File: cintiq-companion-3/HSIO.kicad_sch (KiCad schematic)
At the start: 14 parts, among them J3 Bus_M.2_Socket_M, J4 Bus_M.2_Socket_E

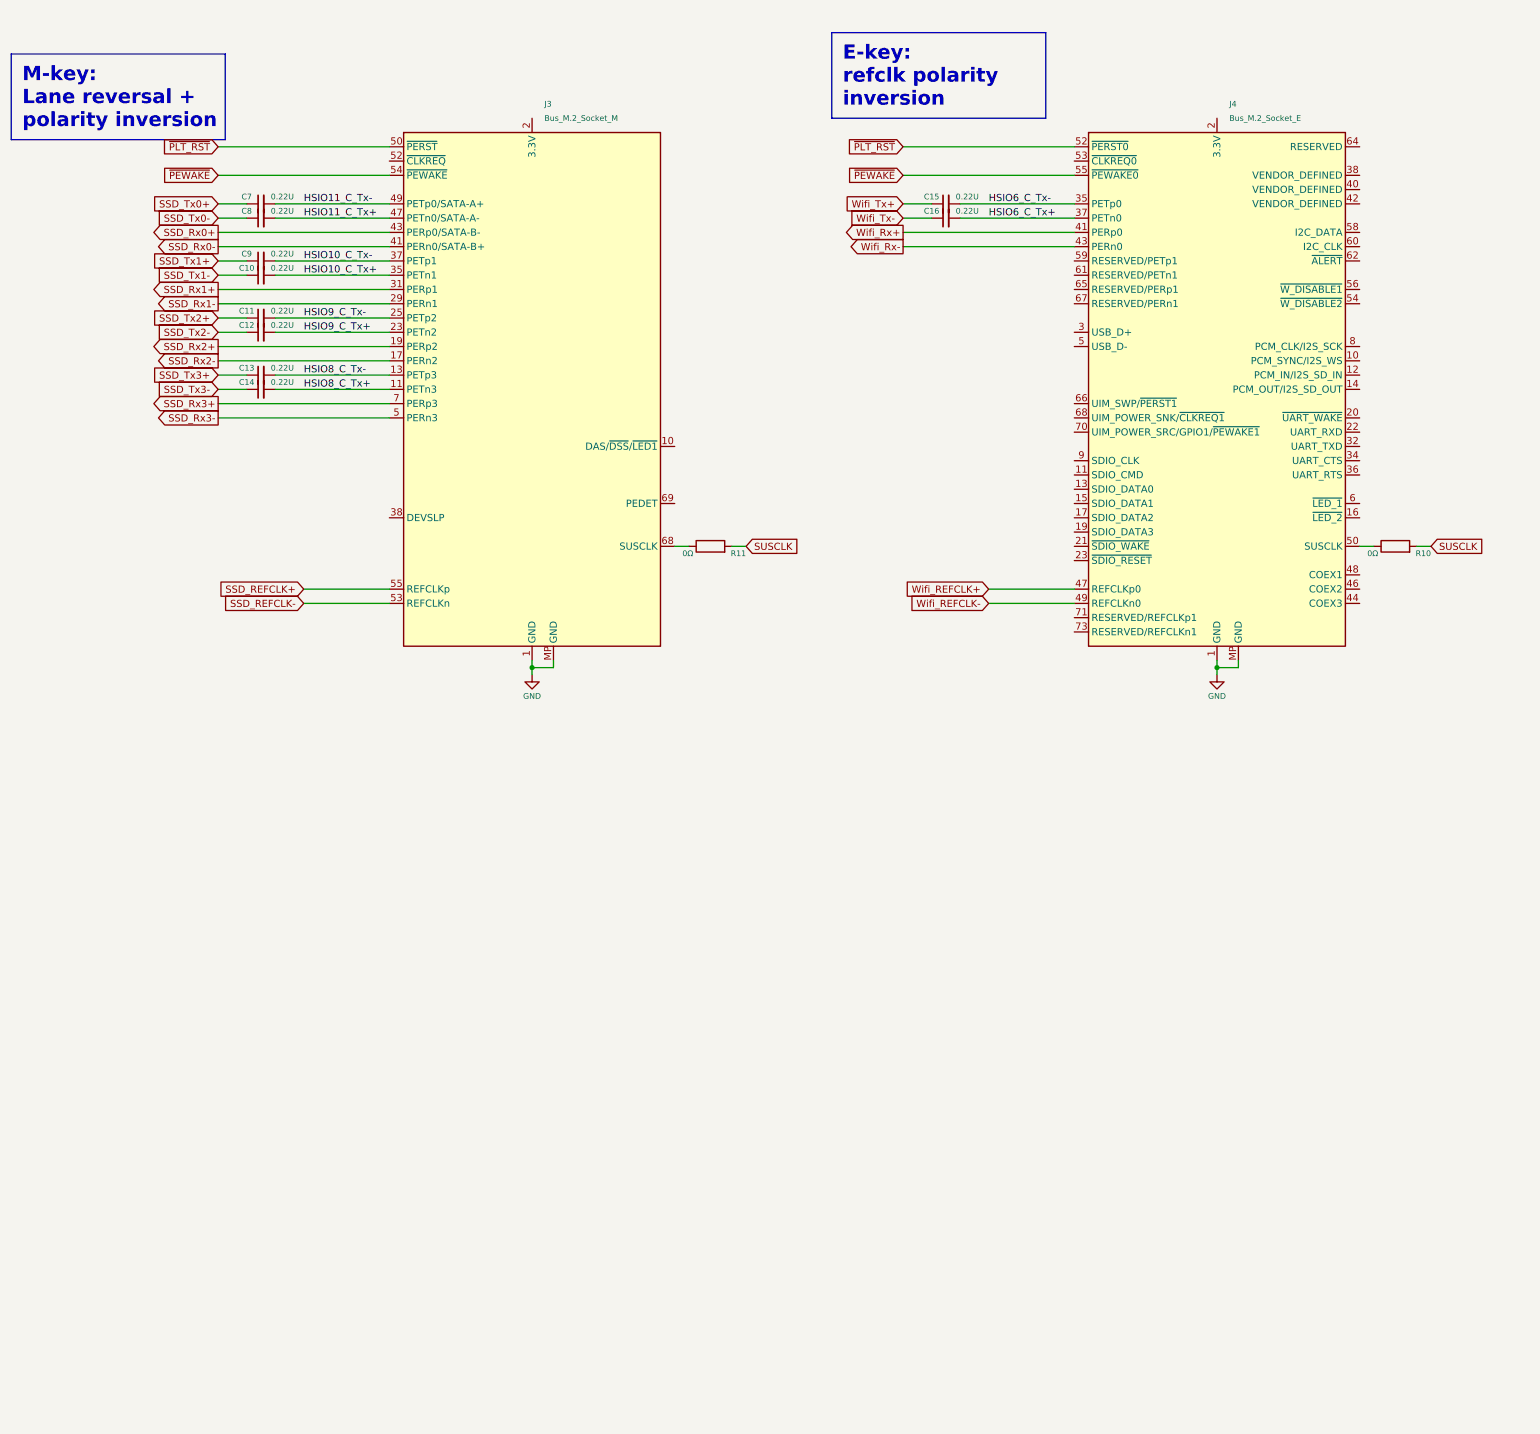
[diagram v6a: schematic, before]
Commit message: Added B-key slot and dual bios chips
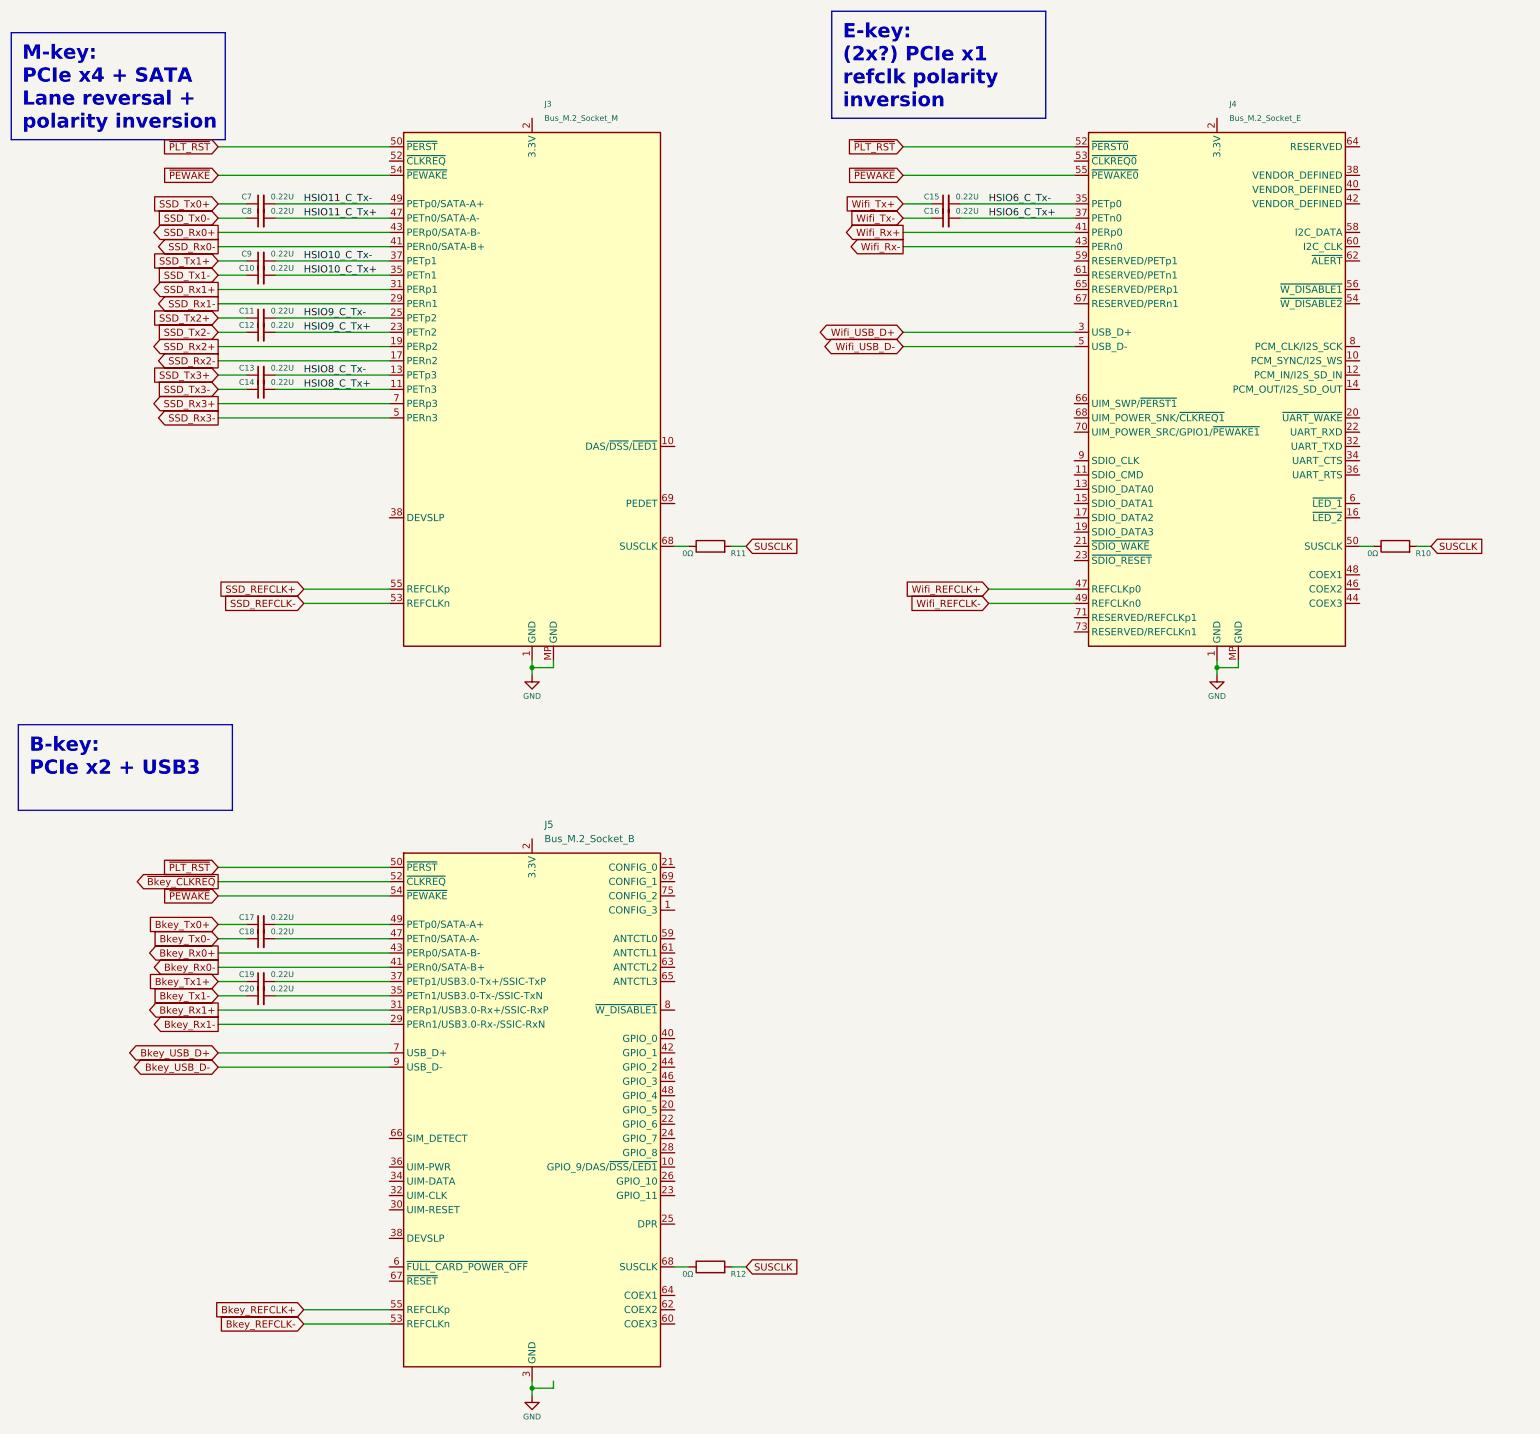
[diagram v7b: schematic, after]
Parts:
- added C17, C18, C19, C20: 0.22U, Capacitor_SMD:C_0402_1005Metric, symbol Device:C_Small
- added J5: Bus_M.2_Socket_B, symbol Connector:Bus_M.2_Socket_B
- added R12: 0Ω, Resistor_SMD:R_0402_1005Metric, symbol Device:R
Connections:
- net GND: now also J5.11 (GND), J5.27 (GND), J5.3 (GND), J5.33 (GND), J5.39 (GND), J5.45 (GND), J5.5 (GND), J5.51 (GND), J5.57 (GND), J5.71 (GND), J5.73 (GND)
- net SUSCLK: now also R12.2
- net ~{PEWAKE}: now also J5.54 (~{PEWAKE})
- net ~{PLT_RST}: now also J5.50 (~{PERST})
- net Wifi_USB_D+: now reaches J4.3 (USB_D+)
- net Wifi_USB_D-: now reaches J4.5 (USB_D-)
- new net: J5.68 (SUSCLK), R12.1
- new net: C20.2, J5.35 (PETn1/USB3.0-Tx-/SSIC-TxN)
- new net: C17.2, J5.49 (PETp0/SATA-A+)
- new net: C18.2, J5.47 (PETn0/SATA-A-)
- new net: C19.2, J5.37 (PETp1/USB3.0-Tx+/SSIC-TxP)
- new net: J5.2 (3.3V), J5.4 (3.3V), J5.70 (3.3V), J5.72 (3.3V), J5.74 (3.3V)
- new net Bkey_REFCLK+: J5.55 (REFCLKp)
- new net Bkey_REFCLK-: J5.53 (REFCLKn)
- new net Bkey_Rx0+: J5.43 (PERp0/SATA-B-)
- new net Bkey_Rx0-: J5.41 (PERn0/SATA-B+)
- new net Bkey_Rx1+: J5.31 (PERp1/USB3.0-Rx+/SSIC-RxP)
- new net Bkey_Rx1-: J5.29 (PERn1/USB3.0-Rx-/SSIC-RxN)
- new net Bkey_Tx0+: C17.1
- new net Bkey_Tx0-: C18.1
- new net Bkey_Tx1+: C19.1
- new net Bkey_Tx1-: C20.1
- new net Bkey_USB_D+: J5.7 (USB_D+)
- new net Bkey_USB_D-: J5.9 (USB_D-)
- new net ~{Bkey_CLKREQ}: J5.52 (~{CLKREQ})

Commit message: Added USB3 and 2nd E-key link
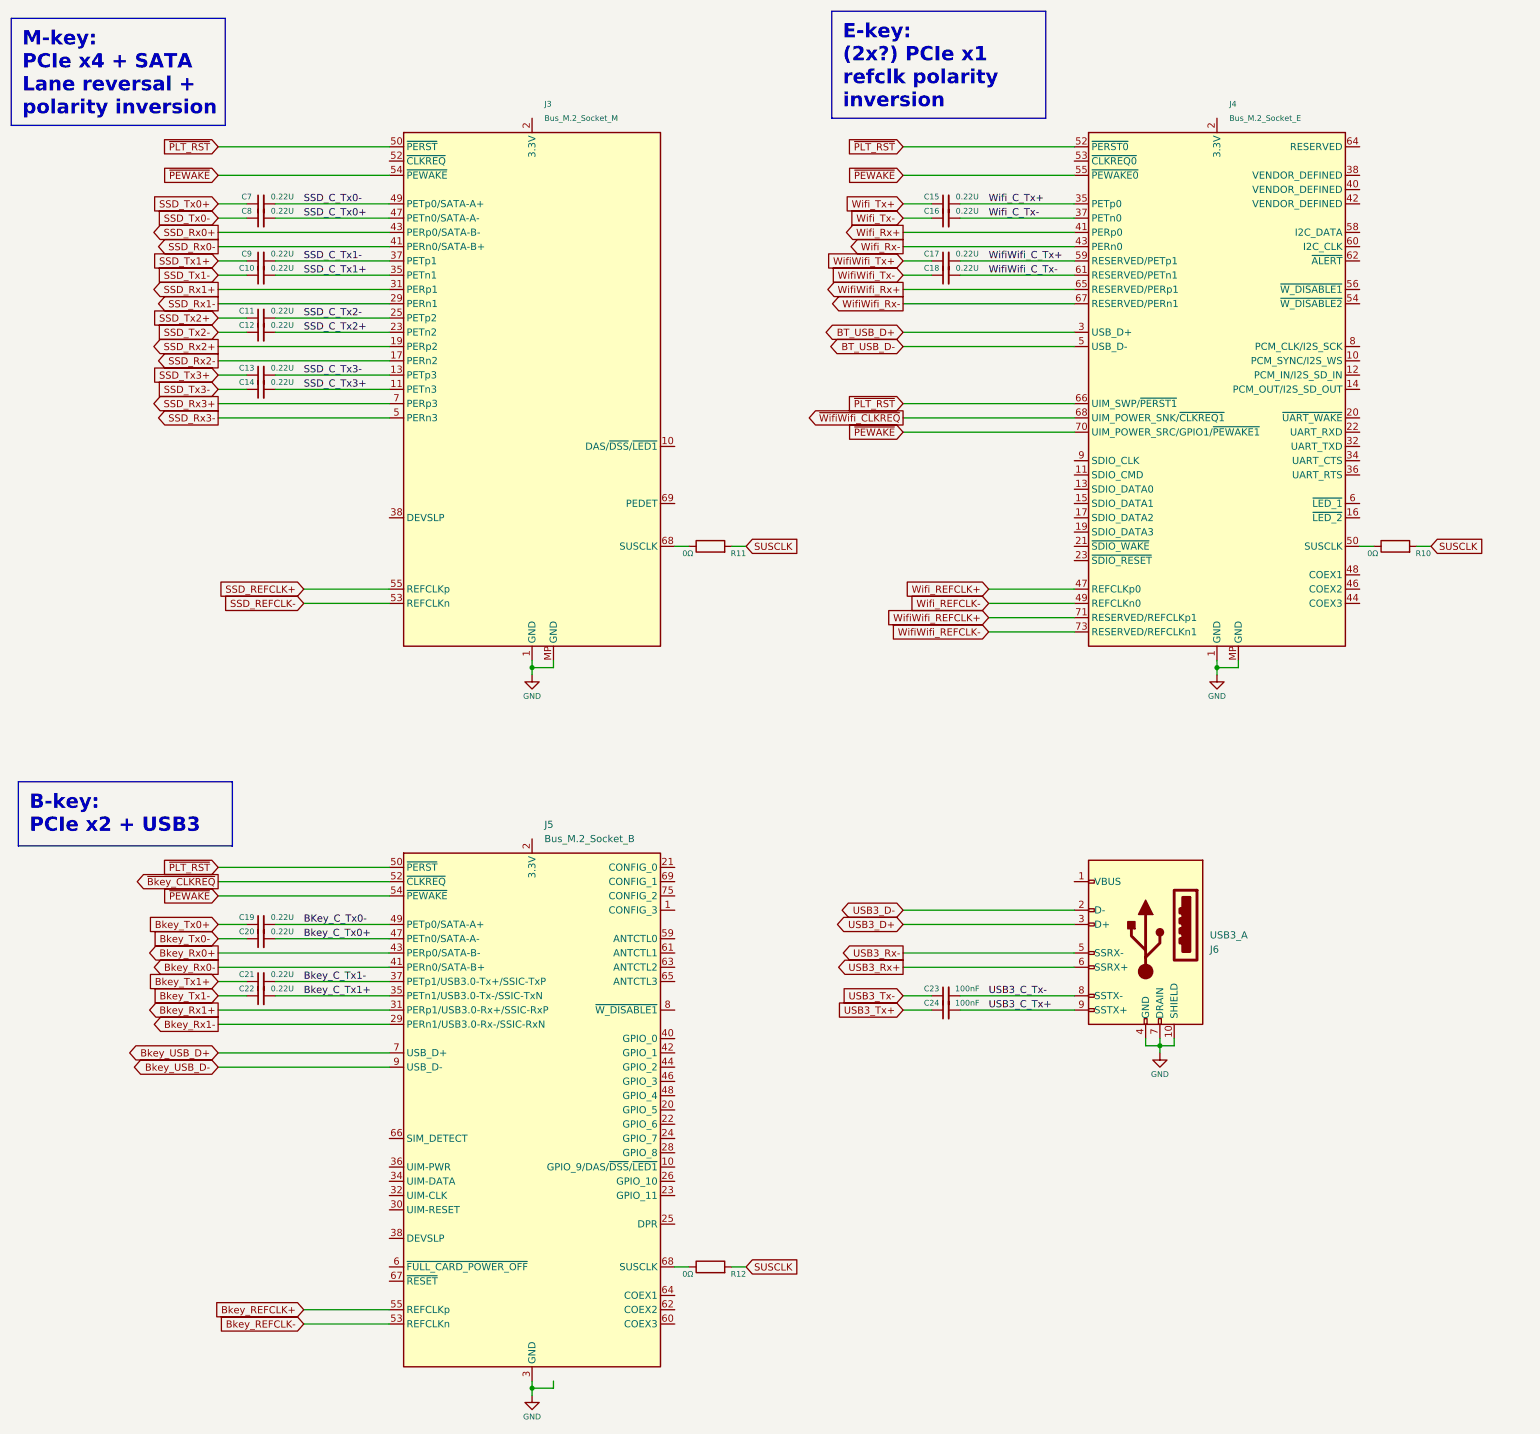
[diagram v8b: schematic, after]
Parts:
- added C21, C22: 0.22U, Capacitor_SMD:C_0402_1005Metric, symbol Device:C_Small
- added C23, C24: 100nF, Capacitor_SMD:C_0402_1005Metric, symbol Device:C_Small
- added J6: USB3_A, symbol Connector:USB3_A
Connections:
- net Bkey_Tx0+: now also C19.1; no longer C17.1
- net Bkey_Tx0-: now also C20.1; no longer C18.1
- net Bkey_Tx1+: now also C21.1; no longer C19.1
- net Bkey_Tx1-: now also C22.1; no longer C20.1
- net GND: now also J6.10 (SHIELD), J6.4 (GND), J6.7 (DRAIN)
- net ~{PEWAKE}: now also J4.70 (UIM_POWER_SRC/GPIO1/~{PEWAKE1})
- net ~{PLT_RST}: now also J4.66 (UIM_SWP/~{PERST1})
- net Bkey_C_Tx0+: now reaches C20.2
- net Bkey_C_Tx0+: now also J5.47 (PETn0/SATA-A-); no longer J5.35 (PETn1/USB3.0-Tx-/SSIC-TxN)
- net WifiWifi_C_Tx+: now reaches J4.59 (RESERVED/PETp1)
- net WifiWifi_C_Tx+: now also C17.2
- net WifiWifi_C_Tx-: now reaches J4.61 (RESERVED/PETn1)
- net WifiWifi_C_Tx-: now also C18.2
- net WifiWifi_Rx+: now reaches J4.65 (RESERVED/PERp1)
- net WifiWifi_Rx-: now reaches J4.67 (RESERVED/PERn1)
- net ~{WifiWifi_CLKREQ}: now reaches J4.68 (UIM_POWER_SNK/~{CLKREQ1})
- net WifiWifi_REFCLK+: now reaches J4.71 (RESERVED/REFCLKp1)
- net WifiWifi_REFCLK-: now reaches J4.73 (RESERVED/REFCLKn1)
- net BKey_C_Tx0-: now reaches J5.49 (PETp0/SATA-A+)
- net BKey_C_Tx0-: now also C19.2; no longer C17.2
- net Bkey_C_Tx1-: now reaches J5.37 (PETp1/USB3.0-Tx+/SSIC-TxP)
- net Bkey_C_Tx1-: now also C21.2; no longer C19.2
- net HSIO10_C_Tx+ renamed SSD_C_Tx1+
- net HSIO10_C_Tx- renamed SSD_C_Tx1-
- net HSIO11_C_Tx+ renamed SSD_C_Tx0+
- net HSIO11_C_Tx- renamed SSD_C_Tx0-
- net HSIO6_C_Tx+ renamed Wifi_C_Tx-
- net HSIO6_C_Tx- renamed Wifi_C_Tx+
- net HSIO8_C_Tx+ renamed SSD_C_Tx3+
- net HSIO8_C_Tx- renamed SSD_C_Tx3-
- net HSIO9_C_Tx+ renamed SSD_C_Tx2+
- net HSIO9_C_Tx- renamed SSD_C_Tx2-
- net Wifi_USB_D+ renamed BT_USB_D+
- net Wifi_USB_D- renamed BT_USB_D-
- new net Bkey_C_Tx1+: C22.2, J5.35 (PETn1/USB3.0-Tx-/SSIC-TxN)
- new net USB3_C_Tx+: C24.2, J6.9 (SSTX+)
- new net USB3_C_Tx-: C23.2, J6.8 (SSTX-)
- new net USB3_D+: J6.3 (D+)
- new net USB3_D-: J6.2 (D-)
- new net USB3_Rx+: J6.6 (SSRX+)
- new net USB3_Rx-: J6.5 (SSRX-)
- new net USB3_Tx+: C24.1
- new net USB3_Tx-: C23.1
- new net WifiWifi_Tx+: C17.1
- new net WifiWifi_Tx-: C18.1
